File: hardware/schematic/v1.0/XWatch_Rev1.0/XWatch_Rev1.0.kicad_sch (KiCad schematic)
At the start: 0 parts

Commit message: Add MCU and display connector symbols, UFBGA-169 footprint, LCSC STM32L4R9AII6 import and schematic sheets
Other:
- added sheet Display (Display.kicad_sch)
- added sheet MCU (MCU.kicad_sch)
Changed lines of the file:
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@@
 	(generator_version "10.0")
 	(paper "A4")
+	(sheet
+		(at 166.37 99.06)
+		(size 20.32 29.21)
+		(exclude_from_sim no)
+		(in_bom yes)
+		(on_board yes)
+		(dnp no)
+		(fields_autoplaced yes)
+		(stroke
+			(width 0.1524)
+			(type solid)
+		)
+		(fill
+			(color 0 0 0 0)
+		)
+		(property "Sheetname" "Display"
+			(at 166.37 98.3484 0)
+			(show_name no)
+			(do_not_autoplace no)
+			(effects
+				(font
+					(size 1.27 1.27)
+				)
+				(justify left bottom)
+			)
+		)
+		(property "Sheetfile" "Display.kicad_sch"
+			(at 166.37 128.8546 0)
+			(show_name no)
+			(do_not_autoplace no)
+			(effects
+				(font
+					(size 1.27 1.27)
+				)
+				(justify left top)
+			)
+		)
+		(instances
+			(project "XWatch_Rev1.0"
+				(path "/2e5e9480-7d2e-4148-a9bf-0ac7d46b20bc"
+					(page "3")
+				)
+			)
+		)
+	)
+	(sheet
+		(at 105.41 95.25)
+		(size 17.78 39.37)
+		(exclude_from_sim no)
+		(in_bom yes)
+		(on_board yes)
+		(dnp no)
+		(fields_autoplaced yes)
+		(stroke
+			(width 0.1524)
+			(type solid)
+		)
+		(fill
+			(color 0 0 0 0)
+		)
+		(property "Sheetname" "MCU"
+			(at 105.41 94.5384 0)
+			(show_name no)
+			(do_not_autoplace no)
+			(effects
+				(font
+					(size 1.27 1.27)
+				)
+				(justify left bottom)
+			)
+		)
+		(property "Sheetfile" "MCU.kicad_sch"
+			(at 105.41 135.2046 0)
+			(show_name no)
+			(do_not_autoplace no)
+			(effects
+				(font
+					(size 1.27 1.27)
+				)
+				(justify left top)
+			)
+		)
+		(instances
+			(project "XWatch_Rev1.0"
+				(path "/2e5e9480-7d2e-4148-a9bf-0ac7d46b20bc"
+					(page "2")
+				)
+			)
+		)
+	)
 	(sheet_instances
 		(path "/"

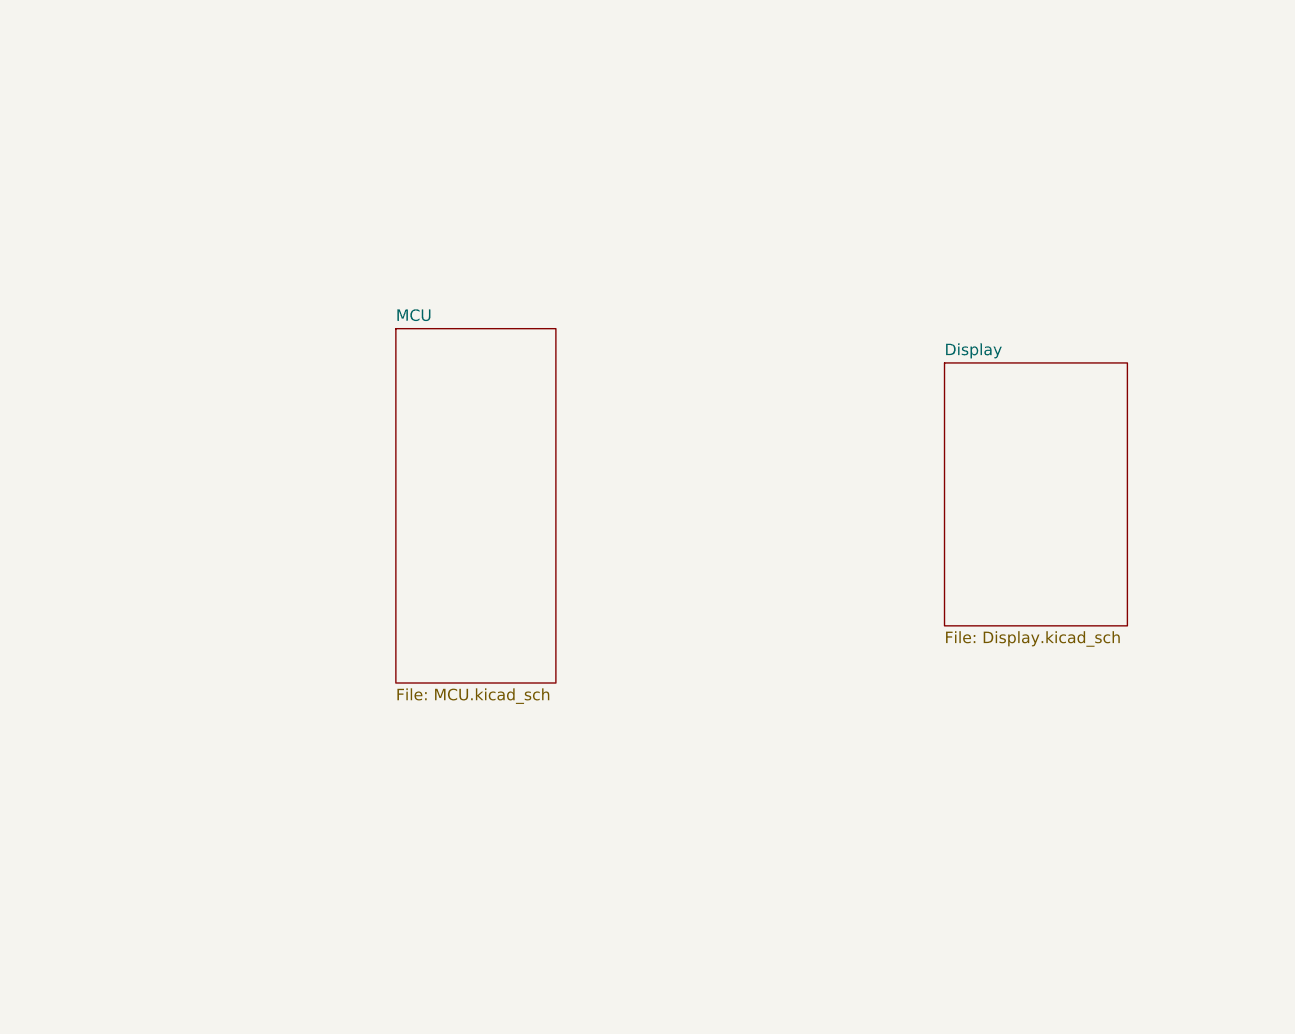
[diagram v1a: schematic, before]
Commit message: Add schematic sub-sheets and component libraries for Rev1.0
- Add Power, GNSS, Sensors, Memory and Connectivity schematic sheets
- Add symbols/footprints for DA9168, SGM38046, MAX86141, BMI270, LSM6DSOX, LIS2MDL, AK09918C, NT3H1101
- Add 3D models for new parts
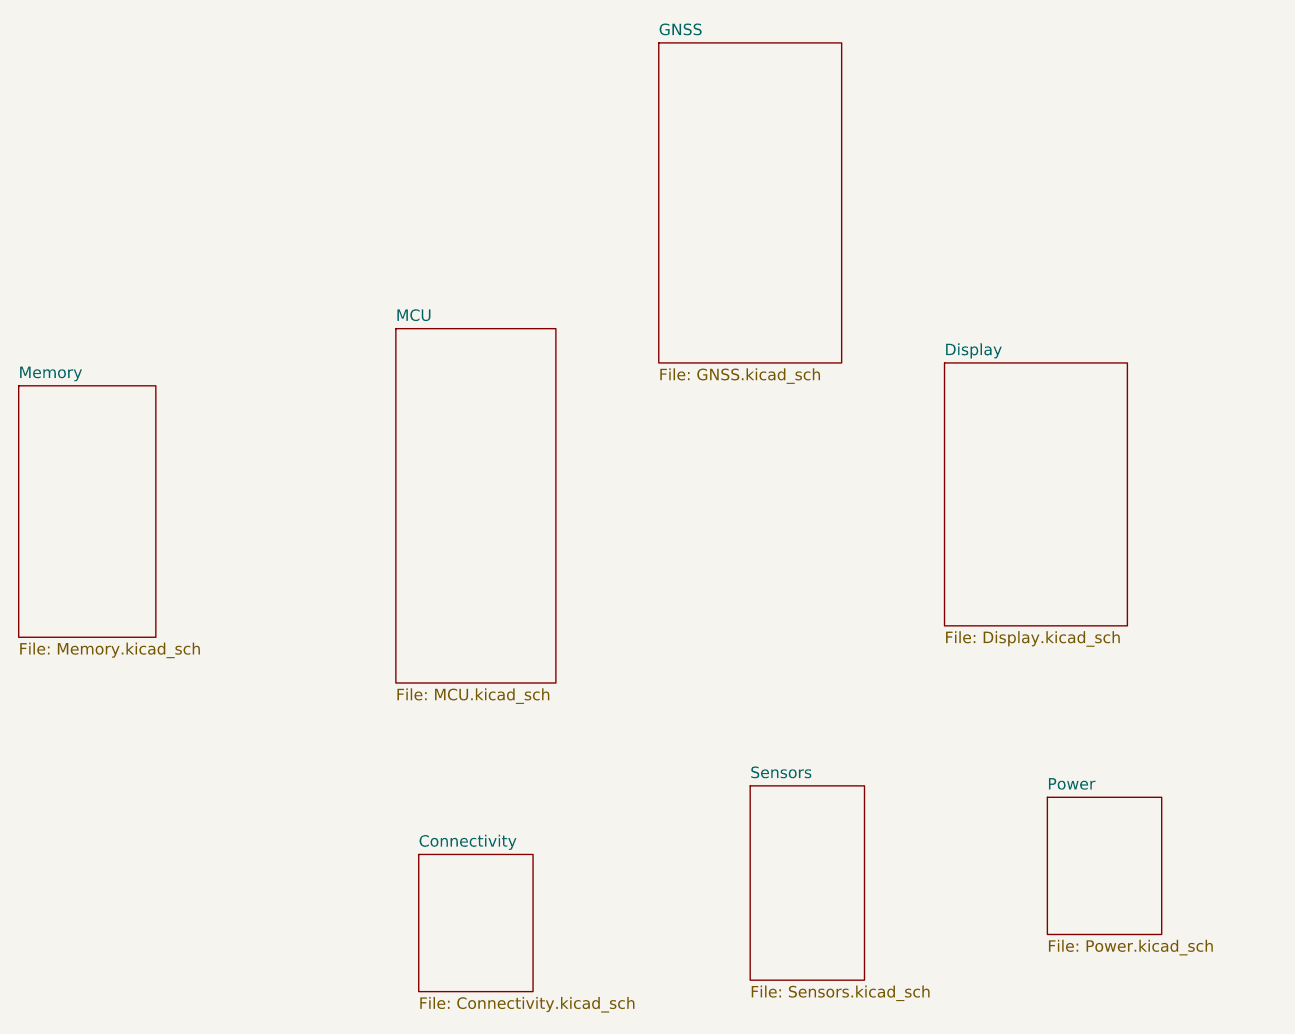
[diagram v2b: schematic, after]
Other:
- added sheet Connectivity (Connectivity.kicad_sch)
- added sheet GNSS (GNSS.kicad_sch)
- added sheet Memory (Memory.kicad_sch)
- added sheet Power (Power.kicad_sch)
- added sheet Sensors (Sensors.kicad_sch)
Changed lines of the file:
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@@
 	(paper "A4")
+	(sheet
+		(at 63.5 101.6)
+		(size 15.24 27.94)
+		(exclude_from_sim no)
+		(in_bom yes)
+		(on_board yes)
+		(dnp no)
+		(fields_autoplaced yes)
+		(stroke
+			(width 0.1524)
+			(type solid)
+		)
+		(fill
+			(color 0 0 0 0)
+		)
+		(property "Sheetname" "Memory"
+			(at 63.5 100.8884 0)
+			(show_name no)
+			(do_not_autoplace no)
+			(effects
+				(font
+					(size 1.27 1.27)
+				)
+				(justify left bottom)
+			)
+		)
+		(property "Sheetfile" "Memory.kicad_sch"
+			(at 63.5 130.1246 0)
+			(show_name no)
+			(do_not_autoplace no)
+			(effects
+				(font
+					(size 1.27 1.27)
+				)
+				(justify left top)
+			)
+		)
+		(instances
+			(project "XWatch_Rev1.0"
+				(path "/2e5e9480-7d2e-4148-a9bf-0ac7d46b20bc"
+					(page "7")
+				)
+			)
+		)
+	)
+	(sheet
+		(at 134.62 63.5)
+		(size 20.32 35.56)
+		(exclude_from_sim no)
+		(in_bom yes)
+		(on_board yes)
+		(dnp no)
+		(fields_autoplaced yes)
+		(stroke
+			(width 0.1524)
+			(type solid)
+		)
+		(fill
+			(color 0 0 0 0)
+		)
+		(property "Sheetname" "GNSS"
+			(at 134.62 62.7884 0)
+			(show_name no)
+			(do_not_autoplace no)
+			(effects
+				(font
+					(size 1.27 1.27)
+				)
+				(justify left bottom)
+			)
+		)
+		(property "Sheetfile" "GNSS.kicad_sch"
+			(at 134.62 99.6446 0)
+			(show_name no)
+			(do_not_autoplace no)
+			(effects
+				(font
+					(size 1.27 1.27)
+				)
+				(justify left top)
+			)
+		)
+		(instances
+			(project "XWatch_Rev1.0"
+				(path "/2e5e9480-7d2e-4148-a9bf-0ac7d46b20bc"
+					(page "8")
+				)
+			)
+		)
+	)
+	(sheet
+		(at 144.78 146.05)
+		(size 12.7 21.59)
+		(exclude_from_sim no)
+		(in_bom yes)
+		(on_board yes)
+		(dnp no)
+		(fields_autoplaced yes)
+		(stroke
+			(width 0.1524)
+			(type solid)
+		)
+		(fill
+			(color 0 0 0 0)
+		)
+		(property "Sheetname" "Sensors"
+			(at 144.78 145.3384 0)
+			(show_name no)
+			(do_not_autoplace no)
+			(effects
+				(font
+					(size 1.27 1.27)
+				)
+				(justify left bottom)
+			)
+		)
+		(property "Sheetfile" "Sensors.kicad_sch"
+			(at 144.78 168.2246 0)
+			(show_name no)
+			(do_not_autoplace no)
+			(effects
+				(font
+					(size 1.27 1.27)
+				)
+				(justify left top)
+			)
+		)
+		(instances
+			(project "XWatch_Rev1.0"
+				(path "/2e5e9480-7d2e-4148-a9bf-0ac7d46b20bc"
+					(page "4")
+				)
+			)
+		)
+	)
+	(sheet
+		(at 177.8 147.32)
+		(size 12.7 15.24)
+		(exclude_from_sim no)
+		(in_bom yes)
+		(on_board yes)
+		(dnp no)
+		(fields_autoplaced yes)
+		(stroke
+			(width 0.1524)
+			(type solid)
+		)
+		(fill
+			(color 0 0 0 0)
+		)
+		(property "Sheetname" "Power"
+			(at 177.8 146.6084 0)
+			(show_name no)
+			(do_not_autoplace no)
+			(effects
+				(font
+					(size 1.27 1.27)
+				)
+				(justify left bottom)
+			)
+		)
+		(property "Sheetfile" "Power.kicad_sch"
+			(at 177.8 163.1446 0)
+			(show_name no)
+			(do_not_autoplace no)
+			(effects
+				(font
+					(size 1.27 1.27)
+				)
+				(justify left top)
+			)
+		)
+		(instances
+			(project "XWatch_Rev1.0"
+				(path "/2e5e9480-7d2e-4148-a9bf-0ac7d46b20bc"
+					(page "6")
+				)
+			)
+		)
+	)
+	(sheet
+		(at 107.95 153.67)
+		(size 12.7 15.24)
+		(exclude_from_sim no)
+		(in_bom yes)
+		(on_board yes)
+		(dnp no)
+		(fields_autoplaced yes)
+		(stroke
+			(width 0.1524)
+			(type solid)
+		)
+		(fill
+			(color 0 0 0 0)
+		)
+		(property "Sheetname" "Connectivity"
+			(at 107.95 152.9584 0)
+			(show_name no)
+			(do_not_autoplace no)
+			(effects
+				(font
+					(size 1.27 1.27)
+				)
+				(justify left bottom)
+			)
+		)
+		(property "Sheetfile" "Connectivity.kicad_sch"
+			(at 107.95 169.4946 0)
+			(show_name no)
+			(do_not_autoplace no)
+			(effects
+				(font
+					(size 1.27 1.27)
+				)
+				(justify left top)
+			)
+		)
+		(instances
+			(project "XWatch_Rev1.0"
+				(path "/2e5e9480-7d2e-4148-a9bf-0ac7d46b20bc"
+					(page "5")
+				)
+			)
+		)
+	)
 	(sheet
 		(at 166.37 99.06)

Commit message: doc and sch update
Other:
- added sheet Audio (Audio.kicad_sch)
- added sheet STLink (STLink.kicad_sch)
- sheet MCU ports: added DSI_BL_CTRL, DSI_SWIRE, DSI_TE, {DSI_LANE}, {DSI_SPI}, {DSI_USART}; removed none
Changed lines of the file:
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@@
 	(generator "eeschema")
 	(generator_version "10.0")
-	(paper "A4")
+	(paper "A3")
 	(sheet
 		(at 63.5 101.6)
@@
 	)
 	(sheet
-		(at 134.62 63.5)
+		(at 287.02 43.18)
 		(size 20.32 35.56)
 		(exclude_from_sim no)
@@
 		)
 		(property "Sheetname" "GNSS"
-			(at 134.62 62.7884 0)
+			(at 287.02 42.4684 0)
 			(show_name no)
 			(do_not_autoplace no)
@@
 		)
 		(property "Sheetfile" "GNSS.kicad_sch"
-			(at 134.62 99.6446 0)
+			(at 287.02 79.3246 0)
 			(show_name no)
 			(do_not_autoplace no)
@@
 	)
 	(sheet
-		(at 144.78 146.05)
+		(at 297.18 125.73)
 		(size 12.7 21.59)
 		(exclude_from_sim no)
@@
 		)
 		(property "Sheetname" "Sensors"
-			(at 144.78 145.3384 0)
+			(at 297.18 125.0184 0)
 			(show_name no)
 			(do_not_autoplace no)
@@
 		)
 		(property "Sheetfile" "Sensors.kicad_sch"
-			(at 144.78 168.2246 0)
+			(at 297.18 147.9046 0)
 			(show_name no)
 			(do_not_autoplace no)
@@
 	)
 	(sheet
-		(at 177.8 147.32)
+		(at 330.2 127)
 		(size 12.7 15.24)
 		(exclude_from_sim no)
@@
 		)
 		(property "Sheetname" "Power"
-			(at 177.8 146.6084 0)
+			(at 330.2 126.2884 0)
 			(show_name no)
 			(do_not_autoplace no)
@@
 		)
 		(property "Sheetfile" "Power.kicad_sch"
-			(at 177.8 163.1446 0)
+			(at 330.2 142.8246 0)
 			(show_name no)
 			(do_not_autoplace no)
@@
 	)
 	(sheet
-		(at 107.95 153.67)
+		(at 339.09 177.8)
 		(size 12.7 15.24)
 		(exclude_from_sim no)
@@
 		)
 		(property "Sheetname" "Connectivity"
-			(at 107.95 152.9584 0)
+			(at 339.09 177.0884 0)
 			(show_name no)
 			(do_not_autoplace no)
@@
 		)
 		(property "Sheetfile" "Connectivity.kicad_sch"
-			(at 107.95 169.4946 0)
+			(at 339.09 193.6246 0)
 			(show_name no)
 			(do_not_autoplace no)
@@
 	)
 	(sheet
-		(at 166.37 99.06)
-		(size 20.32 29.21)
+		(at 142.24 127)
+		(size 35.56 17.78)
 		(exclude_from_sim no)
 		(in_bom yes)
@@
 		)
 		(property "Sheetname" "Display"
-			(at 166.37 98.3484 0)
+			(at 142.24 126.2884 0)
 			(show_name no)
 			(do_not_autoplace no)
@@
 		)
 		(property "Sheetfile" "Display.kicad_sch"
-			(at 166.37 128.8546 0)
+			(at 142.24 145.3646 0)
 			(show_name no)
 			(do_not_autoplace no)
@@
 	)
 	(sheet
-		(at 105.41 95.25)
-		(size 17.78 39.37)
+		(at 80.01 57.15)
+		(size 12.7 21.59)
+		(exclude_from_sim no)
+		(in_bom yes)
+		(on_board yes)
+		(dnp no)
+		(fields_autoplaced yes)
+		(stroke
+			(width 0.1524)
+			(type solid)
+		)
+		(fill
+			(color 0 0 0 0)
+		)
+		(property "Sheetname" "STLink"
+			(at 80.01 56.4384 0)
+			(show_name no)
+			(do_not_autoplace no)
+			(effects
+				(font
+					(size 1.27 1.27)
+				)
+				(justify left bottom)
+			)
+		)
+		(property "Sheetfile" "STLink.kicad_sch"
+			(at 80.01 79.3246 0)
+			(show_name no)
+			(do_not_autoplace no)
+			(effects
+				(font
+					(size 1.27 1.27)
+				)
+				(justify left top)
+			)
+		)
+		(instances
+			(project "XWatch_Rev1.0"
+				(path "/2e5e9480-7d2e-4148-a9bf-0ac7d46b20bc"
+					(page "10")
+				)
+			)
+		)
+	)
+	(sheet
+		(at 368.3 53.34)
+		(size 20.32 26.67)
+		(exclude_from_sim no)
+		(in_bom yes)
+		(on_board yes)
+		(dnp no)
+		(fields_autoplaced yes)
+		(stroke
+			(width 0.1524)
+			(type solid)
+		)
+		(fill
+			(color 0 0 0 0)
+		)
+		(property "Sheetname" "Audio"
+			(at 368.3 52.6284 0)
+			(show_name no)
+			(do_not_autoplace no)
+			(effects
+				(font
+					(size 1.27 1.27)
+				)
+				(justify left bottom)
+			)
+		)
+		(property "Sheetfile" "Audio.kicad_sch"
+			(at 368.3 80.5946 0)
+			(show_name no)
+			(do_not_autoplace no)
+			(effects
+				(font
+					(size 1.27 1.27)
+				)
+				(justify left top)
+			)
+		)
+		(instances
+			(project "XWatch_Rev1.0"
+				(path "/2e5e9480-7d2e-4148-a9bf-0ac7d46b20bc"
+					(page "9")
+				)
+			)
+		)
+	)
+	(sheet
+		(at 189.23 46.99)
+		(size 74.93 210.82)
 		(exclude_from_sim no)
 		(in_bom yes)
@@
 		)
 		(property "Sheetname" "MCU"
-			(at 105.41 94.5384 0)
+			(at 189.23 46.2784 0)
 			(show_name no)
 			(do_not_autoplace no)
@@
 		)
 		(property "Sheetfile" "MCU.kicad_sch"
-			(at 105.41 135.2046 0)
-			(show_name no)
-			(do_not_autoplace no)
-			(effects
-				(font
-					(size 1.27 1.27)
-				)
-				(justify left top)
-			)
-		)
+			(at 189.23 258.3946 0)
+			(show_name no)
+			(do_not_autoplace no)
+			(effects
+				(font
+					(size 1.27 1.27)
+				)
+				(justify left top)
+			)
+		)
+		(pin "{DSI_SPI}" bidirectional
+			(at 189.23 132.08 180)
+			(effects
+				(font
+					(size 1.27 1.27)
+				)
+				(justify left)
+			)
+		)
+		(pin "{DSI_USART}" bidirectional
+			(at 189.23 129.54 180)
+			(effects
+				(font
+					(size 1.27 1.27)
+				)
+				(justify left)
+			)
+		)
+		(pin "{DSI_LANE}" bidirectional
+			(at 189.23 134.62 180)
+			(effects
+				(font
+					(size 1.27 1.27)
+				)
+				(justify left)
+			)
+		)
+		(pin "DSI_TE" output
+			(at 189.23 137.16 180)
+			(effects
+				(font
+					(size 1.27 1.27)
+				)
+				(justify left)
+			)
+		)
+		(pin "DSI_BL_CTRL" bidirectional
+			(at 189.23 139.7 180)
+			(effects
+				(font
+					(size 1.27 1.27)
+				)
+				(justify left)
+			)
+		)
+		(pin "DSI_SWIRE" bidirectional
+			(at 189.23 142.24 180)
+			(effects
+				(font
+					(size 1.27 1.27)
+				)
+				(justify left)
+			)
+		)

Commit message: doc and sch update
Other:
- added sheet DSI_LCD (DSI_LCD.kicad_sch)
- added sheet MCU_IO (MCU_IO.kicad_sch)
- added sheet MCU_PWR (MCU_PWR.kicad_sch)
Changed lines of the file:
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@@
+	)
+	(sheet
+		(at 81.28 245.11)
+		(size 13.97 15.24)
+		(exclude_from_sim no)
+		(in_bom yes)
+		(on_board yes)
+		(dnp no)
+		(fields_autoplaced yes)
+		(stroke
+			(width 0.1524)
+			(type solid)
+		)
+		(fill
+			(color 0 0 0 0)
+		)
+		(property "Sheetname" "MCU_PWR"
+			(at 81.28 244.3984 0)
+			(show_name no)
+			(do_not_autoplace no)
+			(effects
+				(font
+					(size 1.27 1.27)
+				)
+				(justify left bottom)
+			)
+		)
+		(property "Sheetfile" "MCU_PWR.kicad_sch"
+			(at 81.28 260.9346 0)
+			(show_name no)
+			(do_not_autoplace no)
+			(effects
+				(font
+					(size 1.27 1.27)
+				)
+				(justify left top)
+			)
+		)
+		(instances
+			(project "XWatch_Rev1.0"
+				(path "/2e5e9480-7d2e-4148-a9bf-0ac7d46b20bc"
+					(page "13")
+				)
+			)
+		)
+	)
+	(sheet
+		(at 128.27 227.33)
+		(size 15.24 31.75)
+		(exclude_from_sim no)
+		(in_bom yes)
+		(on_board yes)
+		(dnp no)
+		(fields_autoplaced yes)
+		(stroke
+			(width 0.1524)
+			(type solid)
+		)
+		(fill
+			(color 0 0 0 0)
+		)
+		(property "Sheetname" "DSI_LCD"
+			(at 128.27 226.6184 0)
+			(show_name no)
+			(do_not_autoplace no)
+			(effects
+				(font
+					(size 1.27 1.27)
+				)
+				(justify left bottom)
+			)
+		)
+		(property "Sheetfile" "DSI_LCD.kicad_sch"
+			(at 128.27 259.6646 0)
+			(show_name no)
+			(do_not_autoplace no)
+			(effects
+				(font
+					(size 1.27 1.27)
+				)
+				(justify left top)
+			)
+		)
+		(instances
+			(project "XWatch_Rev1.0"
+				(path "/2e5e9480-7d2e-4148-a9bf-0ac7d46b20bc"
+					(page "12")
+				)
+			)
+		)
 	)
 	(sheet
@@
 				)
 			)
+		)
+	)
+	(sheet
+		(at 76.2 190.5)
+		(size 31.75 33.02)
+		(exclude_from_sim no)
+		(in_bom yes)
+		(on_board yes)
+		(dnp no)
+		(fields_autoplaced yes)
+		(stroke
+			(width 0.1524)
+			(type solid)
+		)
+		(fill
+			(color 0 0 0 0)
+		)
+		(property "Sheetname" "MCU_IO"
+			(at 76.2 189.7884 0)
+			(show_name no)
+			(do_not_autoplace no)
+			(effects
+				(font
+					(size 1.27 1.27)
+				)
+				(justify left bottom)
+			)
+		)
+		(property "Sheetfile" "MCU_IO.kicad_sch"
+			(at 76.2 224.1046 0)
+			(show_name no)
+			(do_not_autoplace no)
+			(effects
+				(font
+					(size 1.27 1.27)
+				)
+				(justify left top)
+			)
+		)
+		(instances
+			(project "XWatch_Rev1.0"
+				(path "/2e5e9480-7d2e-4148-a9bf-0ac7d46b20bc"
+					(page "11")
+				)
+			)

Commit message: add rev2.0
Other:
- removed sheet DSI_LCD
- removed sheet MCU_IO
- removed sheet MCU_PWR
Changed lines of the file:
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@@
-	)
-	(sheet
-		(at 81.28 245.11)
-		(size 13.97 15.24)
-		(exclude_from_sim no)
-		(in_bom yes)
-		(on_board yes)
-		(dnp no)
-		(fields_autoplaced yes)
-		(stroke
-			(width 0.1524)
-			(type solid)
-		)
-		(fill
-			(color 0 0 0 0)
-		)
-		(property "Sheetname" "MCU_PWR"
-			(at 81.28 244.3984 0)
-			(show_name no)
-			(do_not_autoplace no)
-			(effects
-				(font
-					(size 1.27 1.27)
-				)
-				(justify left bottom)
-			)
-		)
-		(property "Sheetfile" "MCU_PWR.kicad_sch"
-			(at 81.28 260.9346 0)
-			(show_name no)
-			(do_not_autoplace no)
-			(effects
-				(font
-					(size 1.27 1.27)
-				)
-				(justify left top)
-			)
-		)
-		(instances
-			(project "XWatch_Rev1.0"
-				(path "/2e5e9480-7d2e-4148-a9bf-0ac7d46b20bc"
-					(page "13")
-				)
-			)
-		)
-	)
-	(sheet
-		(at 128.27 227.33)
-		(size 15.24 31.75)
-		(exclude_from_sim no)
-		(in_bom yes)
-		(on_board yes)
-		(dnp no)
-		(fields_autoplaced yes)
-		(stroke
-			(width 0.1524)
-			(type solid)
-		)
-		(fill
-			(color 0 0 0 0)
-		)
-		(property "Sheetname" "DSI_LCD"
-			(at 128.27 226.6184 0)
-			(show_name no)
-			(do_not_autoplace no)
-			(effects
-				(font
-					(size 1.27 1.27)
-				)
-				(justify left bottom)
-			)
-		)
-		(property "Sheetfile" "DSI_LCD.kicad_sch"
-			(at 128.27 259.6646 0)
-			(show_name no)
-			(do_not_autoplace no)
-			(effects
-				(font
-					(size 1.27 1.27)
-				)
-				(justify left top)
-			)
-		)
-		(instances
-			(project "XWatch_Rev1.0"
-				(path "/2e5e9480-7d2e-4148-a9bf-0ac7d46b20bc"
-					(page "12")
-				)
-			)
-		)
 	)
 	(sheet
@@
 				)
 			)
-		)
-	)
-	(sheet
-		(at 76.2 190.5)
-		(size 31.75 33.02)
-		(exclude_from_sim no)
-		(in_bom yes)
-		(on_board yes)
-		(dnp no)
-		(fields_autoplaced yes)
-		(stroke
-			(width 0.1524)
-			(type solid)
-		)
-		(fill
-			(color 0 0 0 0)
-		)
-		(property "Sheetname" "MCU_IO"
-			(at 76.2 189.7884 0)
-			(show_name no)
-			(do_not_autoplace no)
-			(effects
-				(font
-					(size 1.27 1.27)
-				)
-				(justify left bottom)
-			)
-		)
-		(property "Sheetfile" "MCU_IO.kicad_sch"
-			(at 76.2 224.1046 0)
-			(show_name no)
-			(do_not_autoplace no)
-			(effects
-				(font
-					(size 1.27 1.27)
-				)
-				(justify left top)
-			)
-		)
-		(instances
-			(project "XWatch_Rev1.0"
-				(path "/2e5e9480-7d2e-4148-a9bf-0ac7d46b20bc"
-					(page "11")
-				)
-			)
